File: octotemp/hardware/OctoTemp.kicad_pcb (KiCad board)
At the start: 2 copper layers, 47.2 x 34 mm, 48 parts, among them U1 ESP-12E, U2 SPX3819M5, U3 ADC128D818

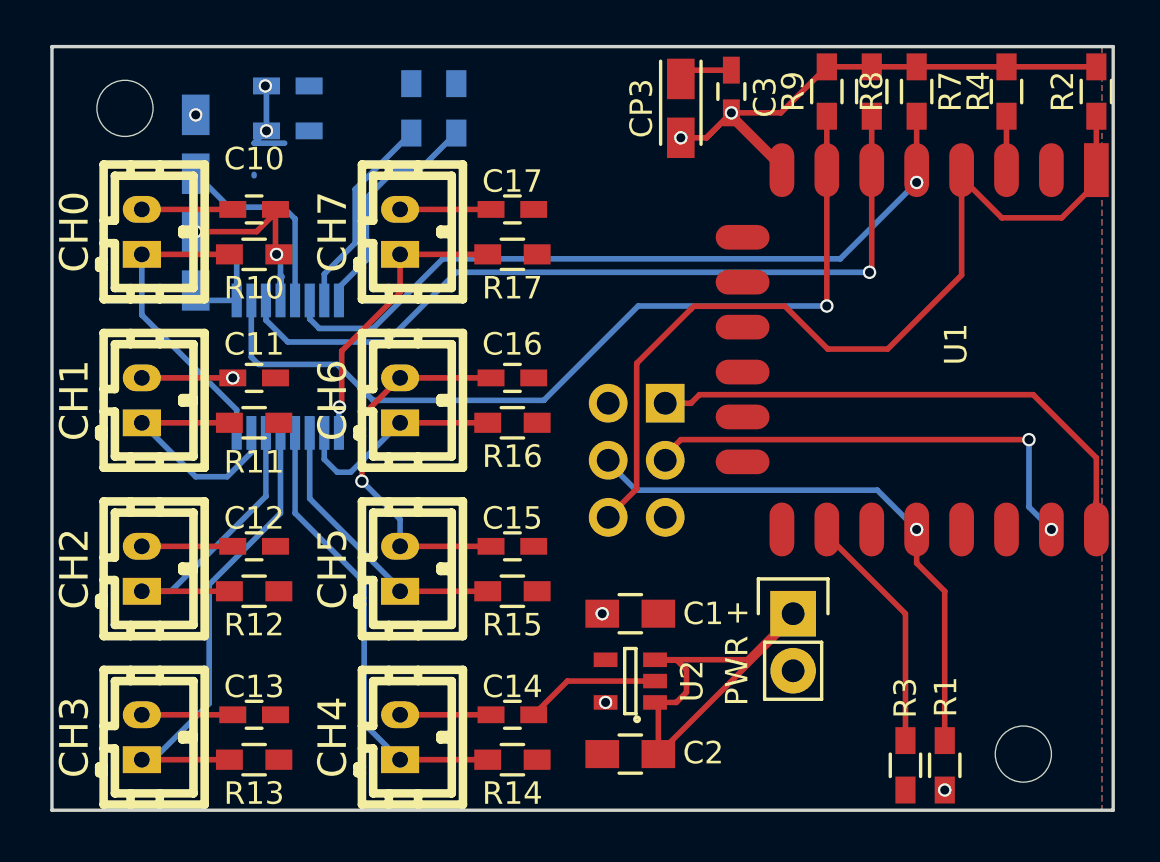
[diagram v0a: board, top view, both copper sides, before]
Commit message: Octotemp board with 2 1x8 pin JST connectors.
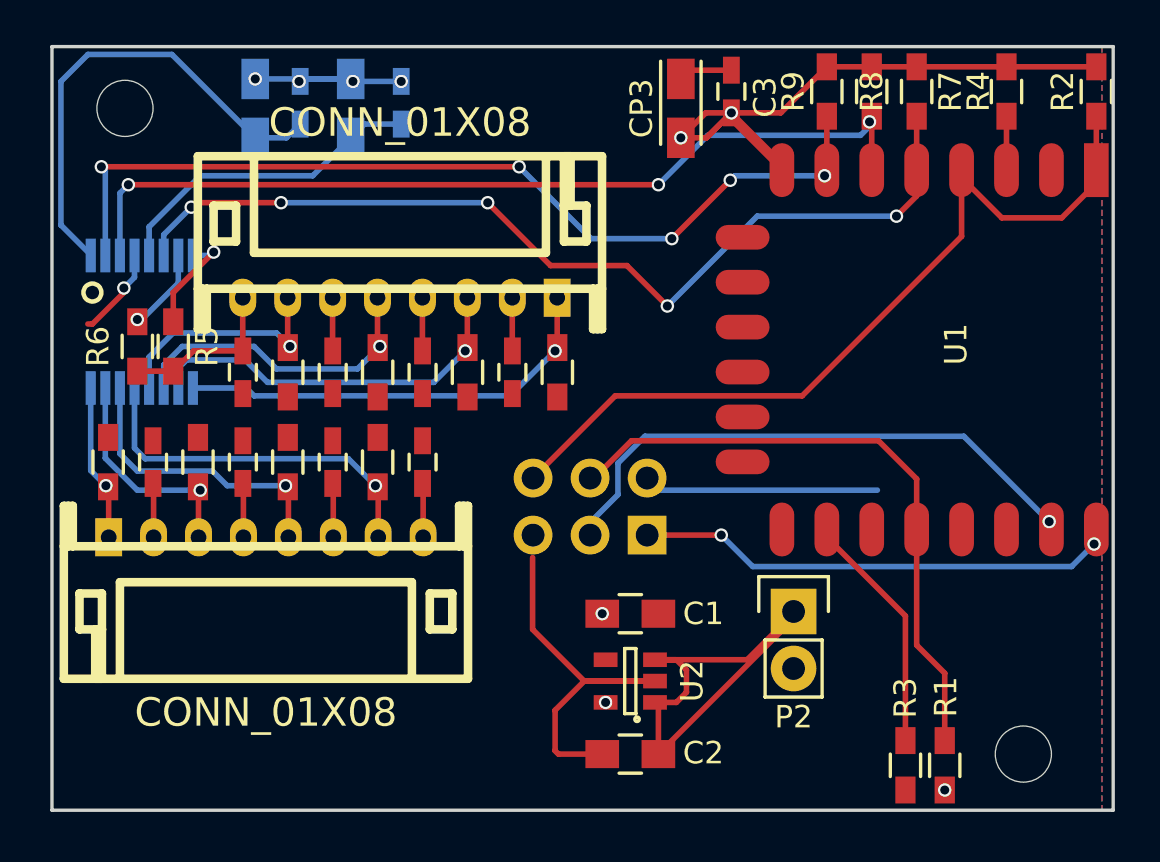
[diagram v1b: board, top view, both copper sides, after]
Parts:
- removed CH0, CH1, CH2, CH3, CH4, CH5, CH6, CH7: CONN_01X02, w_conn_jst-ph:b2b-ph-kl
- removed PROG: CONN_02X03, Pin_Headers:Pin_Header_Straight_2x03
- removed PWR +: CONN_01X02, Pin_Headers:Pin_Header_Straight_1x02
- added P1: CONN_02X03, Pin_Headers:Pin_Header_Straight_2x03, B.Cu at (47.2, 42.3)
- added P2: CONN_01X02, Pin_Headers:Pin_Header_Straight_1x02, F.Cu at (53.8, 45.7)
- added P3: CONN_01X08, w_conn_jst-ph:s8b-ph-kl, F.Cu at (30.3, 42.4)
- added P4: CONN_01X08, w_conn_jst-ph:s8b-ph-kl, F.Cu at (36.2, 31.8)
- R5, R6: moved to F.Cu
- moved R14 19.9 mm to (31.2, 35.1), turned to 270 degrees
- moved C14 19.4 mm to (29.2, 35.1), turned to 90 degrees
- moved R5 16.5 mm to (26.1, 33.9), turned to 90 degrees
- moved R6 16.2 mm to (24.6, 33.9), turned to 90 degrees
- moved R13 14.3 mm to (35.2, 39.1), turned to 90 degrees
- moved C13 13.5 mm to (37.2, 39.1), turned to 270 degrees
- moved C10 12.1 mm to (25.2, 39.1), turned to 270 degrees
- moved R15 11.4 mm to (35.2, 35.1), turned to 270 degrees
- moved R10 11.3 mm to (23.2, 39.1), turned to 90 degrees
- moved C15 11.1 mm to (33.2, 35.1), turned to 90 degrees
- moved CP2 9.69 mm to (34.0, 23.3)
- moved C17 7.25 mm to (41.2, 35.1), turned to 90 degrees
- moved U3 6.80 mm to (24.8, 32.8)
- moved R12 5.94 mm to (31.2, 39.1), turned to 90 degrees
- moved R17 5.62 mm to (43.2, 35.1), turned to 270 degrees
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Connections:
- net IN0 renamed CH0_L
- net IN1 renamed CH1_L
- net IN2 renamed CH2_L
- net IN3 renamed CH3_L
- net IN4 renamed CH4_L
- net IN5 renamed CH5_L
- net IN6 renamed CH6_L
- net IN7 renamed CH7_L
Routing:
- net ADC_VIN: track 83.2 -> 102.1 mm, vias 7 -> 5
- net ADC_GND: track 23.6 -> 34.1 mm
- net CH4_L: track 20.4 -> 10.7 mm, vias 0 -> 1
- net ADC_INT: track 33.8 -> 42.7 mm, vias 1 -> 5
- net CH6_L: track 9.60 -> 17.2 mm, vias 0 -> 1
- net CH0_L: track 13.6 -> 7.01 mm, vias 0 -> 1
- net CH7_L: track 13.0 -> 19.5 mm
- net Net-(R5-Pad2): track 10.3 -> 4.83 mm, vias 0 -> 1
- net Net-(R6-Pad2): track 9.06 -> 3.82 mm, vias 0 -> 1
- net CH3_L: track 21.3 -> 16.5 mm, vias 0 -> 1
- net ESP_RXD: track 21.2 -> 25.5 mm, vias 2 -> 1
- net SCL: track 36.4 -> 40.3 mm, vias 1 -> 3
- net ESP_TXD: track 25.0 -> 21.6 mm, vias 0 -> 2
- net GPIO0: track 25.0 -> 28.3 mm, vias 1 -> 0
- net ESP_RST: track 40.4 -> 37.2 mm
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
